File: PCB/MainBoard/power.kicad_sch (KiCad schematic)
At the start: 16 parts, among them J1 Conn_01x01_Female, J1 Conn_01x02_Male, J2 Conn_01x01_Female, J3 Conn_01x01_Female, U1 uA78MC, U2 L7805

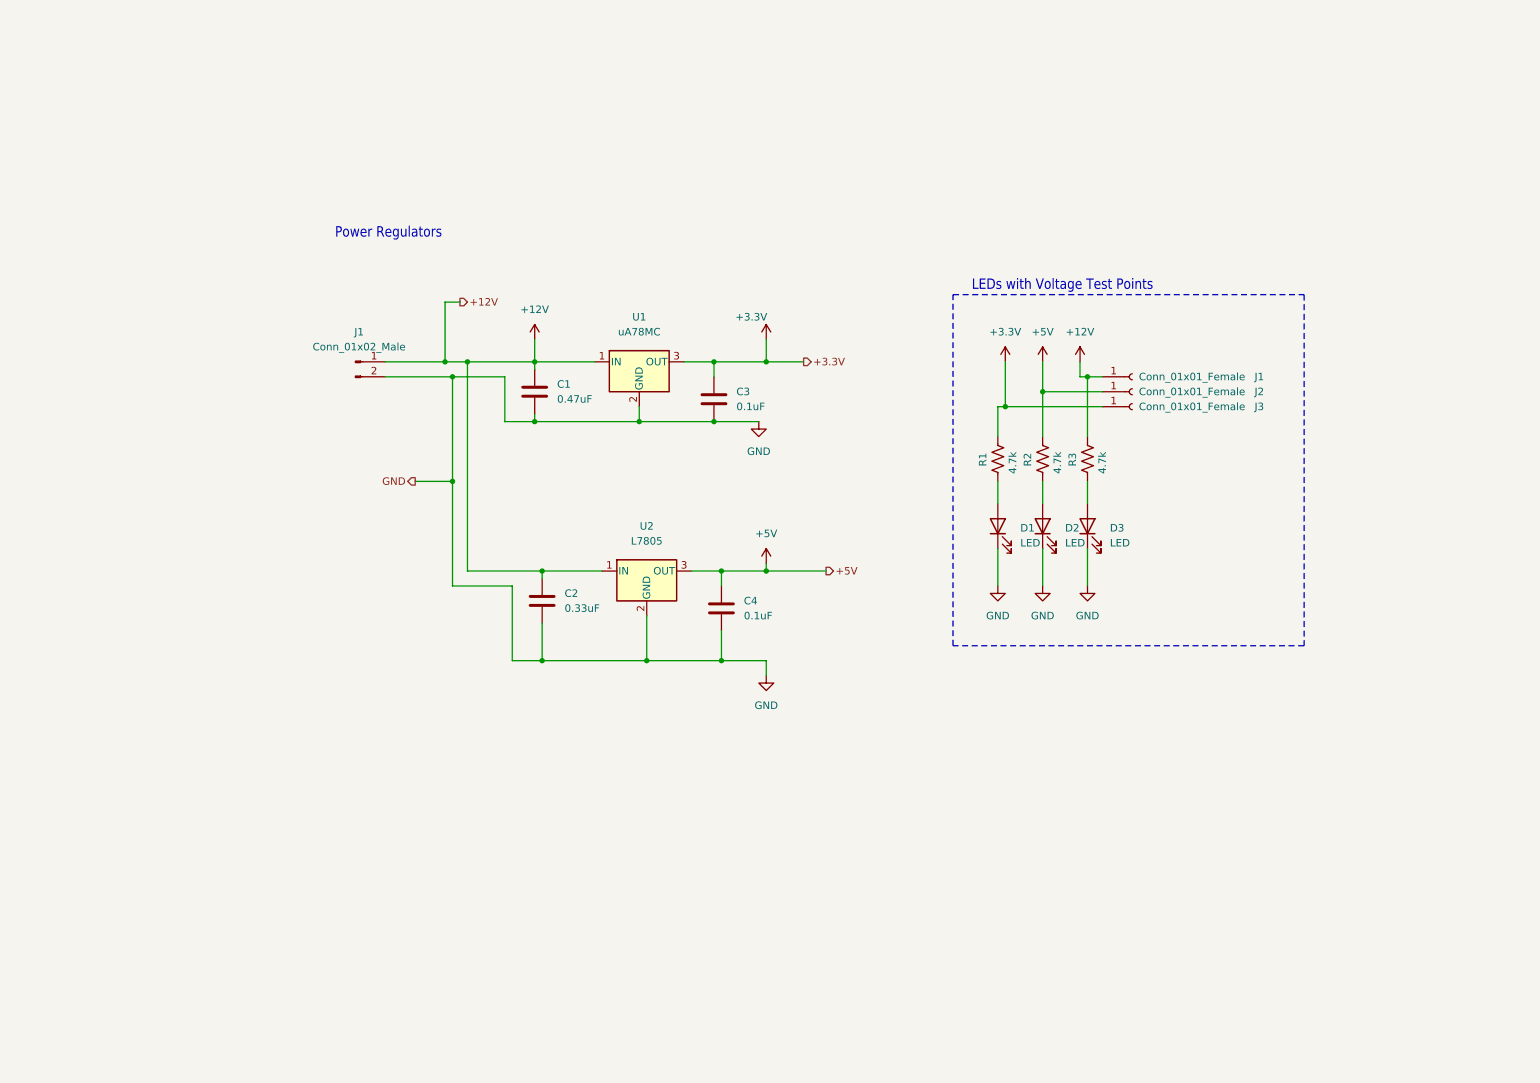
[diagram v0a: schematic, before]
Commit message: updating pcb
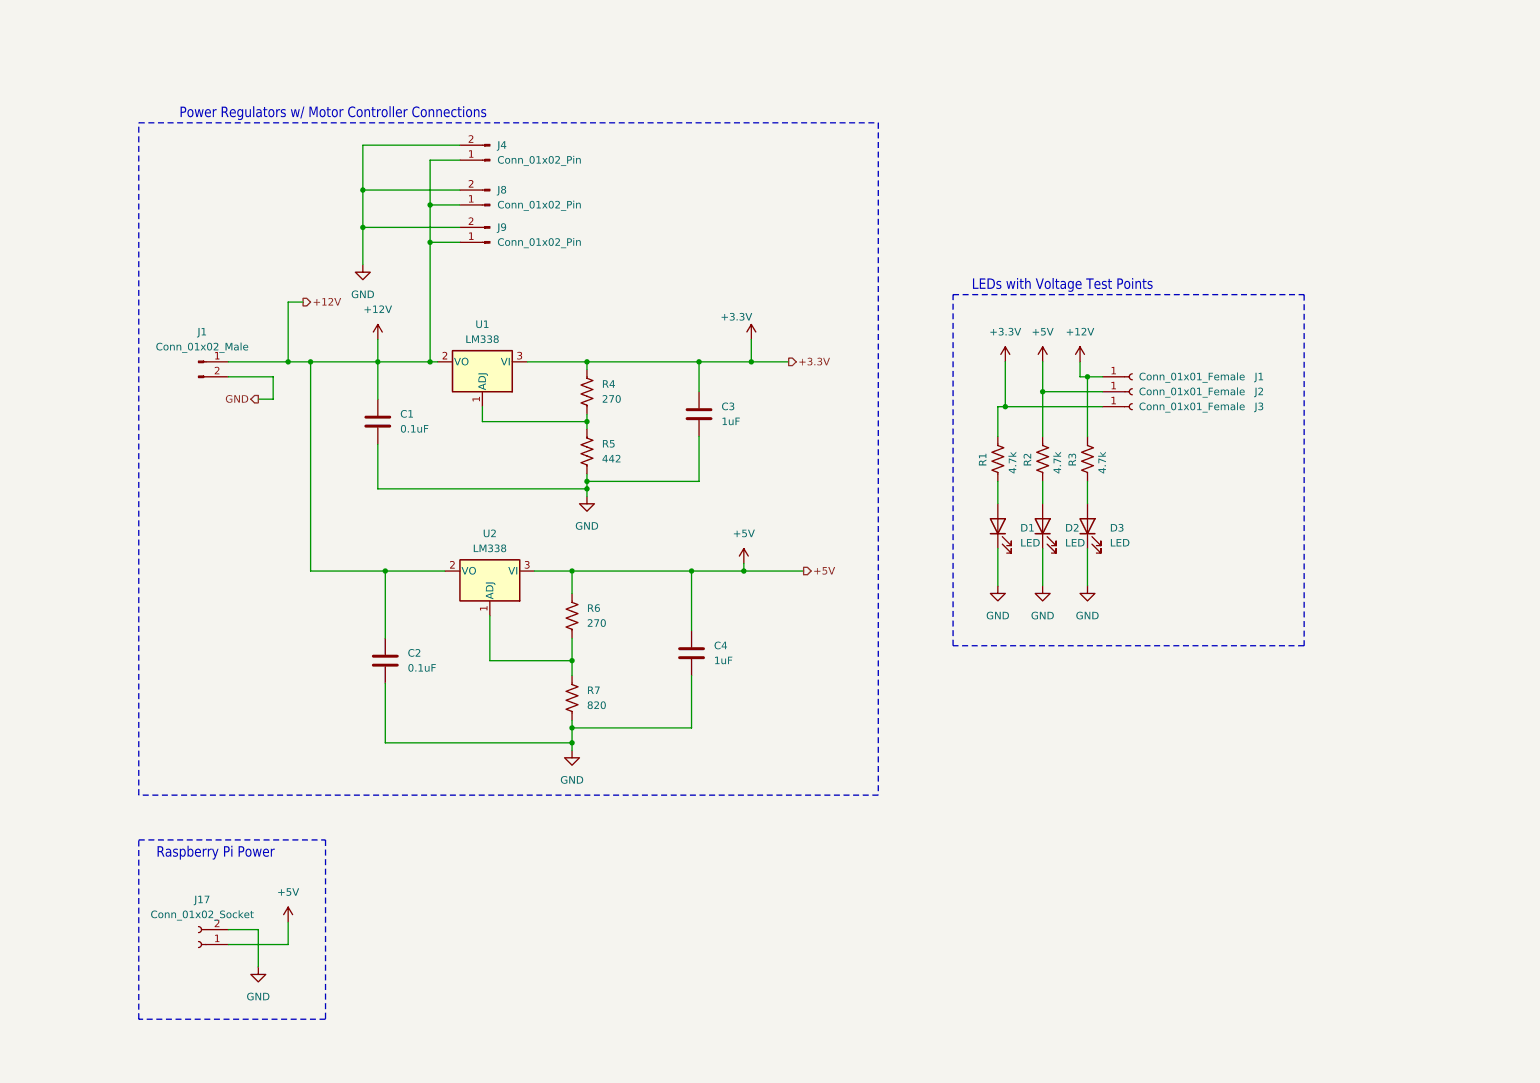
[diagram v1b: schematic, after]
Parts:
- removed U1: uA78MC, Local Footprints:TO-220-3_Horizontal_TabDown, symbol Regulator_Linear:uA7805
- removed U2: L7805, Package_TO_SOT_THT:TO-220-3_Horizontal_TabDown, symbol Regulator_Linear:L7805
- added J17: Conn_01x02_Socket, symbol Connector:Conn_01x02_Socket
- added J4, J8, J9: Conn_01x02_Pin, symbol Connector:Conn_01x02_Pin
- added R4, R6: 270, symbol Device:R_US
- added R5: 442, symbol Device:R_US
- added R7: 820, symbol Device:R_US
- added U1, U2: LM338, Package_TO_SOT_THT:TO-3, symbol Regulator_Linear:LM337_TO3
- C1: value 0.47uF -> 0.1uF
- C2: value 0.33uF -> 0.1uF
- C3, C4: value 0.1uF -> 1uF
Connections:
- net +12V: now also J4.1 (Pin_1), J8.1 (Pin_1), J9.1 (Pin_1), U1.2 (VO), U2.2 (VO)
- net +3.3V: now also R4.1, U1.3 (VI)
- net +5V: now also J17.1 (Pin_1), R6.1, U2.3 (VI)
- net GND: now also J17.2 (Pin_2), J4.2 (Pin_2), J8.2 (Pin_2), J9.2 (Pin_2), R5.2, R7.2
- new net: R6.2, R7.1, U2.1 (ADJ)
- new net: R4.2, R5.1, U1.1 (ADJ)
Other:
- note added: "Power Regulators w/ Motor Controller Connections"
- note added: "Raspberry Pi Power"
- note removed: "Power Regulators"
- moved on the sheet: C1, C2, C3, C4, J1

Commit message: updating progress
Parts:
- removed C1: 0.1uF, Capacitor_THT:C_Disc_D5.0mm_W2.5mm_P5.00mm, symbol Device:C
- removed C2: 0.1uF, Capacitor_SMD:C_1206_3216Metric_Pad1.33x1.80mm_HandSolder, symbol Device:C
- renumbered C3 to C1, C4 to C2
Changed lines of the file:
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@@
 	)
 	(junction
-		(at 83.82 109.22)
-		(diameter 0)
-		(color 0 0 0 0)
-	)
-	(junction
 		(at 80.01 50.8)
 		(diameter 0)
@@
 	)
 	(junction
-		(at 118.11 95.25)
-		(diameter 0)
-		(color 0 0 0 0)
-	)
-	(junction
 		(at 71.12 73.66)
 		(diameter 0)
@@
 	)
 	(junction
-		(at 115.57 138.43)
-		(diameter 0)
-		(color 0 0 0 0)
-	)
-	(junction
 		(at 189.23 81.28)
 		(diameter 0)
@@
 	(wire
 		(pts
-			(xy 83.82 128.27) (xy 83.82 138.43)
-		)
-		(stroke
-			(width 0)
-			(type default)
-		)
-	)
-	(wire
-		(pts
 			(xy 189.23 73.66) (xy 189.23 81.28)
 		)
@@
 	(wire
 		(pts
-			(xy 118.11 96.52) (xy 118.11 95.25)
-		)
-		(stroke
-			(width 0)
-			(type default)
-		)
-	)
-	(wire
-		(pts
 			(xy 91.44 39.37) (xy 91.44 46.99)
 		)
@@
 	(wire
 		(pts
-			(xy 83.82 138.43) (xy 115.57 138.43)
-		)
-		(stroke
-			(width 0)
-			(type default)
-		)
-	)
-	(wire
-		(pts
 			(xy 64.77 76.2) (xy 64.77 80.01)
 		)
@@
 	(wire
 		(pts
-			(xy 82.55 95.25) (xy 118.11 95.25)
-		)
-		(stroke
-			(width 0)
-			(type default)
-		)
-	)
-	(wire
-		(pts
 			(xy 91.44 46.99) (xy 91.44 53.34)
 		)
@@
 	(wire
 		(pts
-			(xy 71.12 109.22) (xy 83.82 109.22)
-		)
-		(stroke
-			(width 0)
-			(type default)
-		)
-	)
-	(wire
-		(pts
 			(xy 187.96 81.28) (xy 189.23 81.28)
 		)
@@
 	(wire
 		(pts
-			(xy 83.82 109.22) (xy 93.98 109.22)
+			(xy 71.12 109.22) (xy 93.98 109.22)
 		)
 		(stroke
@@
 	(wire
 		(pts
-			(xy 82.55 87.63) (xy 82.55 95.25)
-		)
-		(stroke
-			(width 0)
-			(type default)
-		)
-	)
-	(wire
-		(pts
 			(xy 71.12 73.66) (xy 71.12 109.22)
 		)
@@
 	(wire
 		(pts
-			(xy 118.11 95.25) (xy 118.11 93.98)
+			(xy 118.11 93.98) (xy 118.11 96.52)
 		)
 		(stroke
@@
 	(wire
 		(pts
-			(xy 115.57 135.89) (xy 115.57 138.43)
+			(xy 115.57 135.89) (xy 115.57 139.7)
 		)
 		(stroke
@@
 	(wire
 		(pts
-			(xy 115.57 138.43) (xy 115.57 139.7)
-		)
-		(stroke
-			(width 0)
-			(type default)
-		)
-	)
-	(wire
-		(pts
 			(xy 100.33 83.82) (xy 100.33 81.28)
 		)
@@
 	(wire
 		(pts
-			(xy 83.82 109.22) (xy 83.82 120.65)
-		)
-		(stroke
-			(width 0)
-			(type default)
-		)
-	)
-	(wire
-		(pts
 			(xy 91.44 73.66) (xy 82.55 73.66)
 		)
@@
 		)
 	)
-	(wire
-		(pts
-			(xy 82.55 73.66) (xy 82.55 80.01)
-		)
-		(stroke
-			(width 0)
-			(type default)
-		)
-	)
 	(rectangle
 		(start 180.34 62.23)
@@
 		(dnp no)
 		(fields_autoplaced yes)
-		(property "Reference" "C4"
+		(property "Reference" "C2"
 			(at 139.7 121.9199 0)
 			(effects
@@
 			(project "MainBoard"
 				(path "/ce4aa5cc-bc13-46ce-a61c-95c4be48f850/7cb6be40-ad14-404d-82c5-ced68dcd093c"
-					(reference "C4")
+					(reference "C2")
 					(unit 1)
 				)
@@
 		(dnp no)
 		(fields_autoplaced yes)
-		(property "Reference" "C3"
+		(property "Reference" "C1"
 			(at 140.97 81.2799 0)
 			(effects
@@
 			(project "MainBoard"
 				(path "/ce4aa5cc-bc13-46ce-a61c-95c4be48f850/7cb6be40-ad14-404d-82c5-ced68dcd093c"
-					(reference "C3")
+					(reference "C1")
 					(unit 1)
 				)
@@
 	)
 	(symbol
-		(lib_id "Device:C")
-		(at 82.55 83.82 0)
-		(unit 1)
-		(exclude_from_sim no)
-		(in_bom yes)
-		(on_board yes)
-		(dnp no)
-		(fields_autoplaced yes)
-		(property "Reference" "C1"
-			(at 86.36 82.5499 0)
-			(effects
-				(font
-					(size 1.27 1.27)
-				)
-				(justify left)
-			)
-		)
-		(property "Value" "0.1uF"
-			(at 86.36 85.0899 0)
-			(effects
-				(font
-					(size 1.27 1.27)
-				)
-				(justify left)
-			)
-		)
-		(property "Footprint" "Capacitor_THT:C_Disc_D5.0mm_W2.5mm_P5.00mm"
-			(at 83.5152 87.63 0)
-			(effects
-				(font
-					(size 1.27 1.27)
-				)
-				(hide yes)
-			)
-		)
-		(property "Datasheet" "~"
-			(at 82.55 83.82 0)
-			(effects
-				(font
-					(size 1.27 1.27)
-				)
-				(hide yes)
-			)
-		)
-		(property "Description" ""
-			(at 82.55 83.82 0)
-			(effects
-				(font
-					(size 1.27 1.27)
-				)
-				(hide yes)
-			)
-		)
-		(pin "1"
-		)
-		(pin "2"
-		)
-		(instances
-			(project "MainBoard"
-				(path "/ce4aa5cc-bc13-46ce-a61c-95c4be48f850/7cb6be40-ad14-404d-82c5-ced68dcd093c"
-					(reference "C1")
-					(unit 1)
-				)
-			)
-		)
-	)
-	(symbol
 		(lib_id "Connector:Conn_01x02_Male")
 		(at 52.07 73.66 0)
@@
 					(unit 1)
 				)
-			)
-		)
-	)
-	(symbol
-		(lib_id "Device:C")
-		(at 83.82 124.46 0)
-		(unit 1)
-		(exclude_from_sim no)
-		(in_bom yes)
-		(on_board yes)
-		(dnp no)
-		(fields_autoplaced yes)
-		(property "Reference" "C2"
-			(at 87.63 123.1899 0)
-			(effects
-				(font
-					(size 1.27 1.27)
-				)
-				(justify left)
-			)
-		)
-		(property "Value" "0.1uF"
-			(at 87.63 125.7299 0)
-			(effects
-				(font
-					(size 1.27 1.27)
-				)
-				(justify left)
-			)
-		)
-		(property "Footprint" "Capacitor_SMD:C_1206_3216Metric_Pad1.33x1.80mm_HandSolder"
-			(at 84.7852 128.27 0)
-			(effects
-				(font
-					(size 1.27 1.27)
-				)
-				(hide yes)
-			)
-		)
-		(property "Datasheet" "~"
-			(at 83.82 124.46 0)
-			(effects
-				(font
-					(size 1.27 1.27)
-				)
-				(hide yes)
-			)
-		)
-		(property "Description" ""
-			(at 83.82 124.46 0)
-			(effects
-				(font
-					(size 1.27 1.27)
-				)
-				(hide yes)
-			)
-		)
-		(pin "1"
-		)
-		(pin "2"
-		)
-		(instances
-			(project "MainBoard"
-				(path "/ce4aa5cc-bc13-46ce-a61c-95c4be48f850/7cb6be40-ad14-404d-82c5-ced68dcd093c"
-					(reference "C2")
-					(unit 1)
-				)

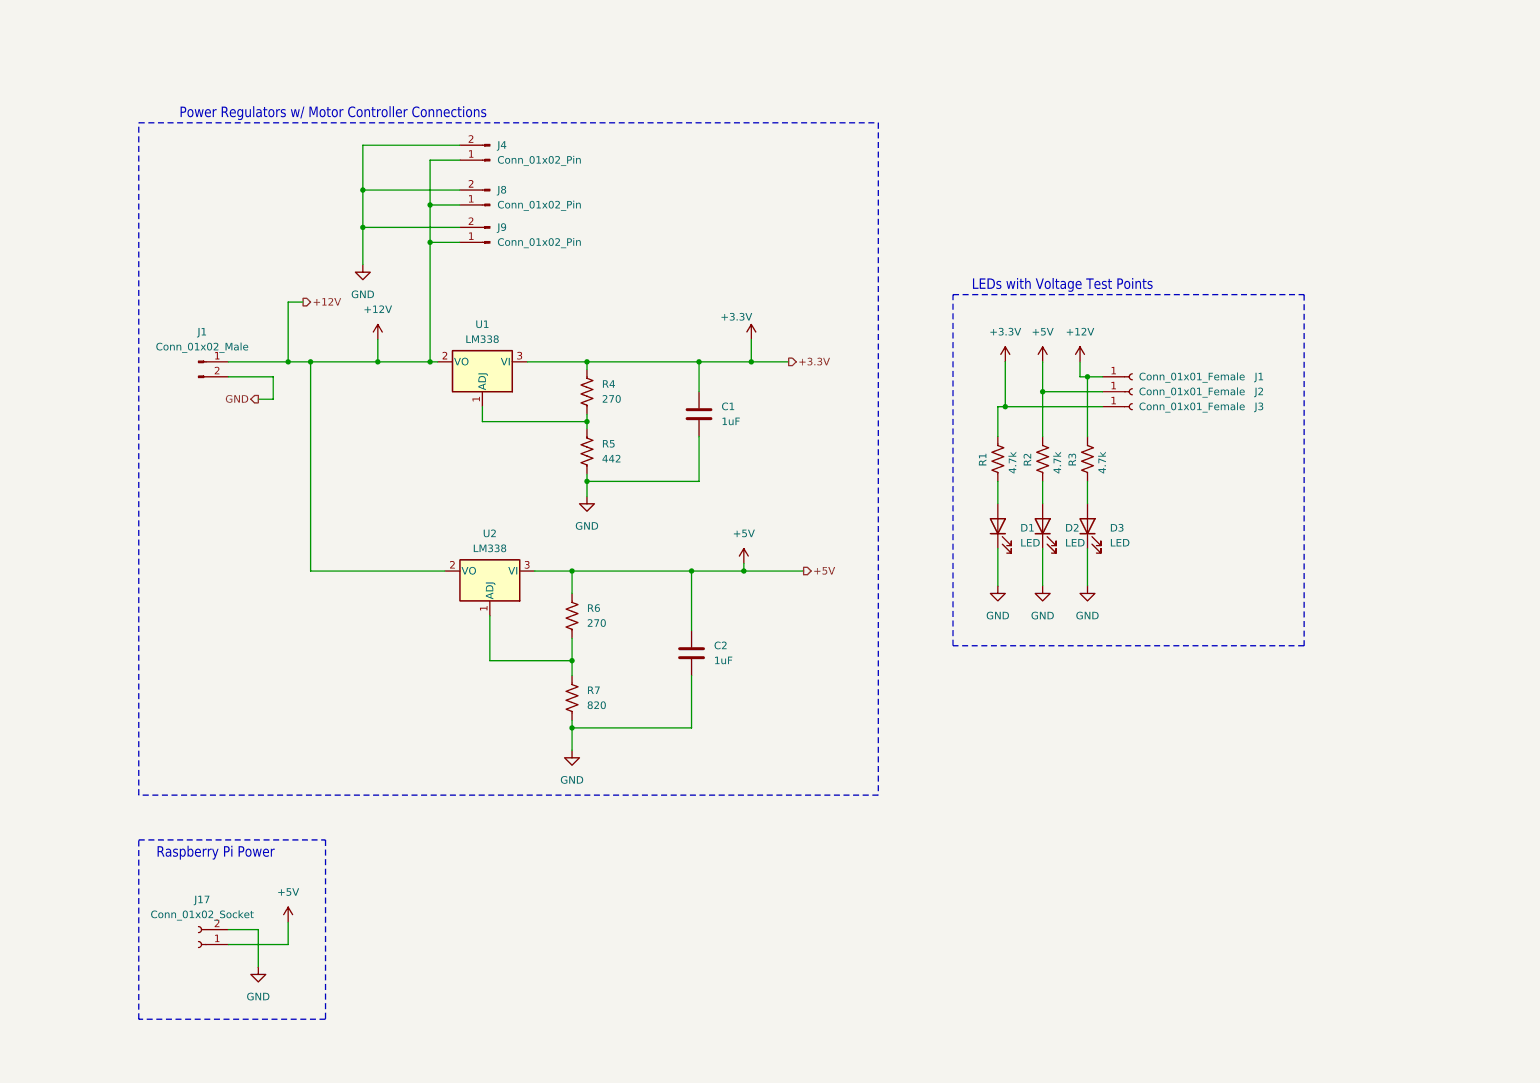
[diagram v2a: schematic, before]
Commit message: adding nazar's work onto new branch
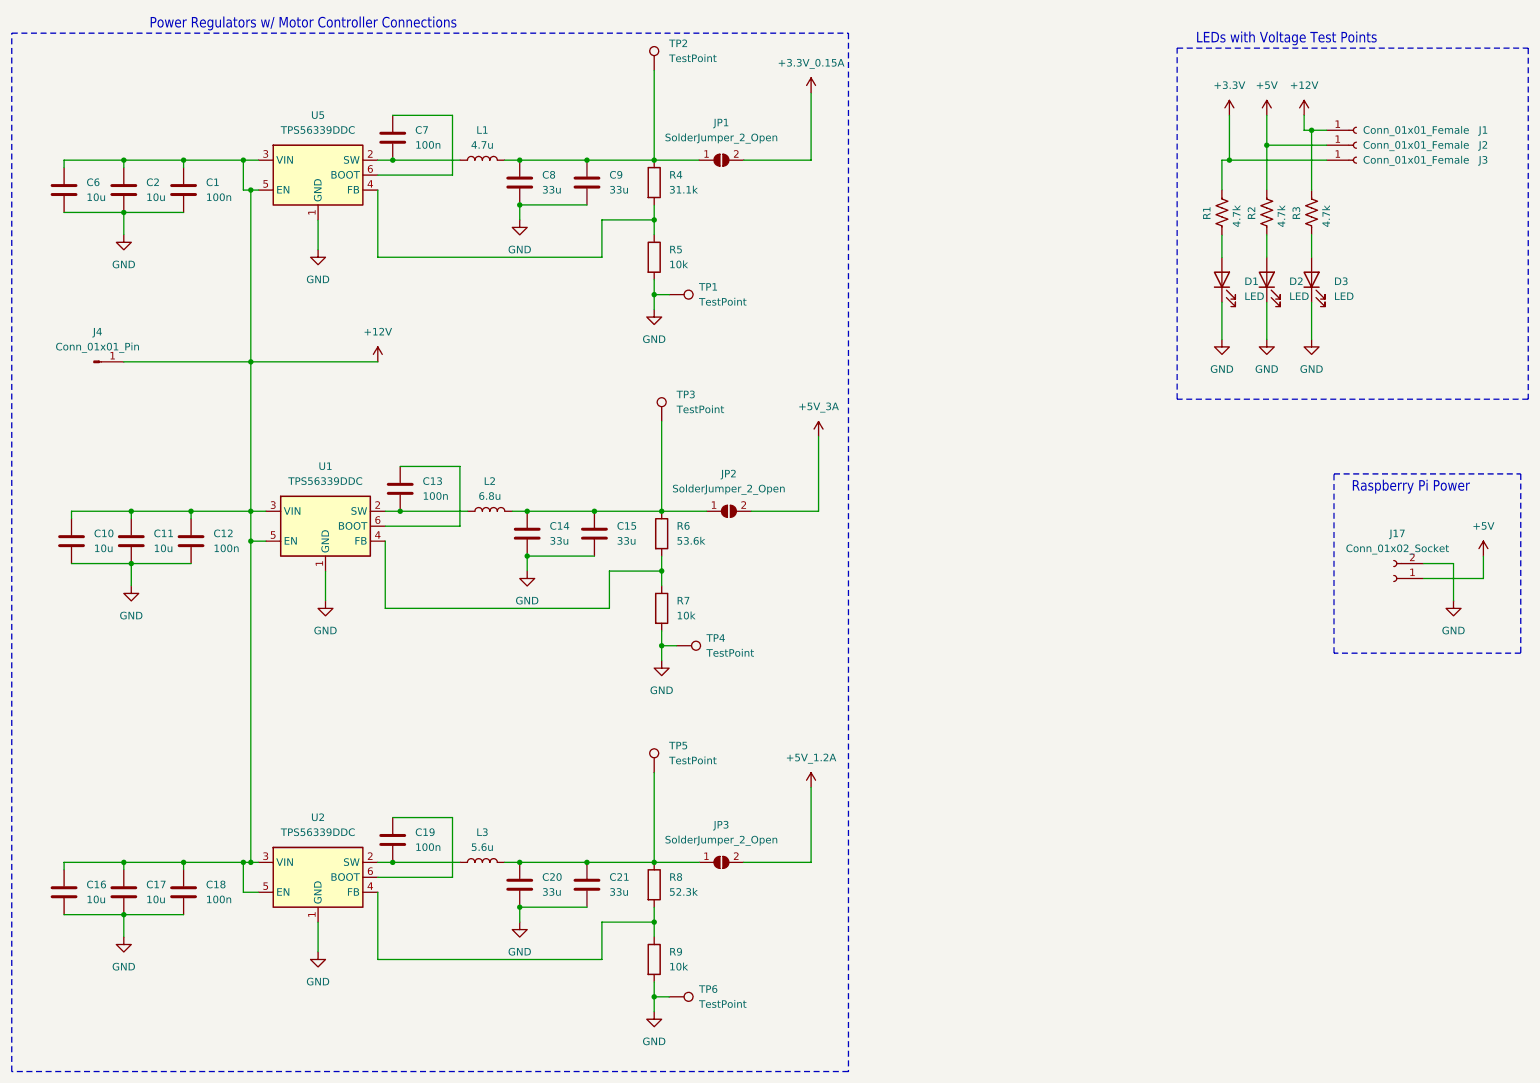
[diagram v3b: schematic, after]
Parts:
- removed J1: Conn_01x02_Male, Connector_Wire:SolderWire-0.5sqmm_1x02_P4.8mm_D0.9mm_OD2.3mm, symbol Connector:Conn_01x02_Male
- removed J4, J8, J9: Conn_01x02_Pin, symbol Connector:Conn_01x02_Pin
- removed R4, R6: 270, symbol Device:R_US
- removed R5: 442, symbol Device:R_US
- removed R7: 820, symbol Device:R_US
- removed U1, U2: LM338, Package_TO_SOT_THT:TO-3, symbol Regulator_Linear:LM337_TO3
- added C10, C11, C16, C17, C6: 10u, symbol Device:C
- added C12, C13, C18, C19, C7: 100n, symbol Device:C
- added C14, C15, C20, C21, C8, C9: 33u, symbol Device:C
- added J4: Conn_01x01_Pin, symbol Connector:Conn_01x01_Pin
- added JP1, JP2, JP3: SolderJumper_2_Open, symbol Jumper:SolderJumper_2_Open
- added L1: 4.7u, symbol Device:L
- added L2: 6.8u, symbol Device:L
- added L3: 5.6u, symbol Device:L
- added R4: 31.1k, symbol Device:R
- added R5, R7, R9: 10k, symbol Device:R
- added R6: 53.6k, symbol Device:R
- added R8: 52.3k, symbol Device:R
- added TP1, TP2, TP3, TP4, TP5, TP6: TestPoint, symbol Connector:TestPoint
- added U1, U2, U5: TPS56339DDC, Package_TO_SOT_SMD:SOT-23-6, symbol Regulator_Switching:TPS56339DDC
- C1: value 1uF -> 100n; footprint Capacitor_SMD:C_0805_2012Metric_Pad1.18x1.45mm_HandSolder -> (none)
- C2: value 1uF -> 10u; footprint Capacitor_SMD:C_0805_2012Metric_Pad1.18x1.45mm_HandSolder -> (none)
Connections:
- net +12V: now also C1.1, C2.1, C10.1, C11.1, C12.1, C16.1, C17.1, C18.1, C6.1, J4.1 (Pin_1), U1.3 (VIN), U1.5 (EN), U2.3 (VIN), U2.5 (EN), U5.3 (VIN), U5.5 (EN)
- net +3.3V: no longer C1.1
- net +5V: no longer C2.1
- net GND: now also C10.2, C11.2, C12.2, C14.2, C15.2, C16.2, C17.2, C18.2, C20.2, C21.2, C6.2, C8.2, C9.2, R5.2, R7.2, R9.2, TP1.1, TP4.1, TP6.1, U1.1 (GND), U2.1 (GND), U5.1 (GND)
- new net: C8.1, C9.1, JP1.1 (A), L1.2, R4.1, TP2.1
- new net: R4.2, R5.1, U5.4 (FB)
- new net: C14.1, C15.1, JP2.1 (A), L2.2, R6.1, TP3.1
- new net: R8.2, R9.1, U2.4 (FB)
- new net: R6.2, R7.1, U1.4 (FB)
- new net: C20.1, C21.1, JP3.1 (A), L3.2, R8.1, TP5.1
- new net: C7.1, U5.6 (BOOT)
- new net: C7.2, L1.1, U5.2 (SW)
- new net: C13.2, L2.1, U1.2 (SW)
- new net: C13.1, U1.6 (BOOT)
- new net: C19.1, U2.6 (BOOT)
- new net: C19.2, L3.1, U2.2 (SW)
- new net +3.3V_0.15A: JP1.2 (B)
- new net +5V_1.2A: JP3.2 (B)
- new net +5V_3A: JP2.2 (B)
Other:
- moved on the sheet: D1, D2, D3, J1, J17, J2, J3, R1, R2, R3
